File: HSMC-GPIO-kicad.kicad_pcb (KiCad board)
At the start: 2 copper layers, 88.9 x 78.1 mm, 158 parts, among them J1 HSMC, J3 Conn_01x03_Male, J4 I2C, J5 Screw_Terminal_01x04, J6 Conn_02x20_Odd_Even, J7 Conn_02x20_Odd_Even, U2 MC78M05_TO252, U3 TCA9517

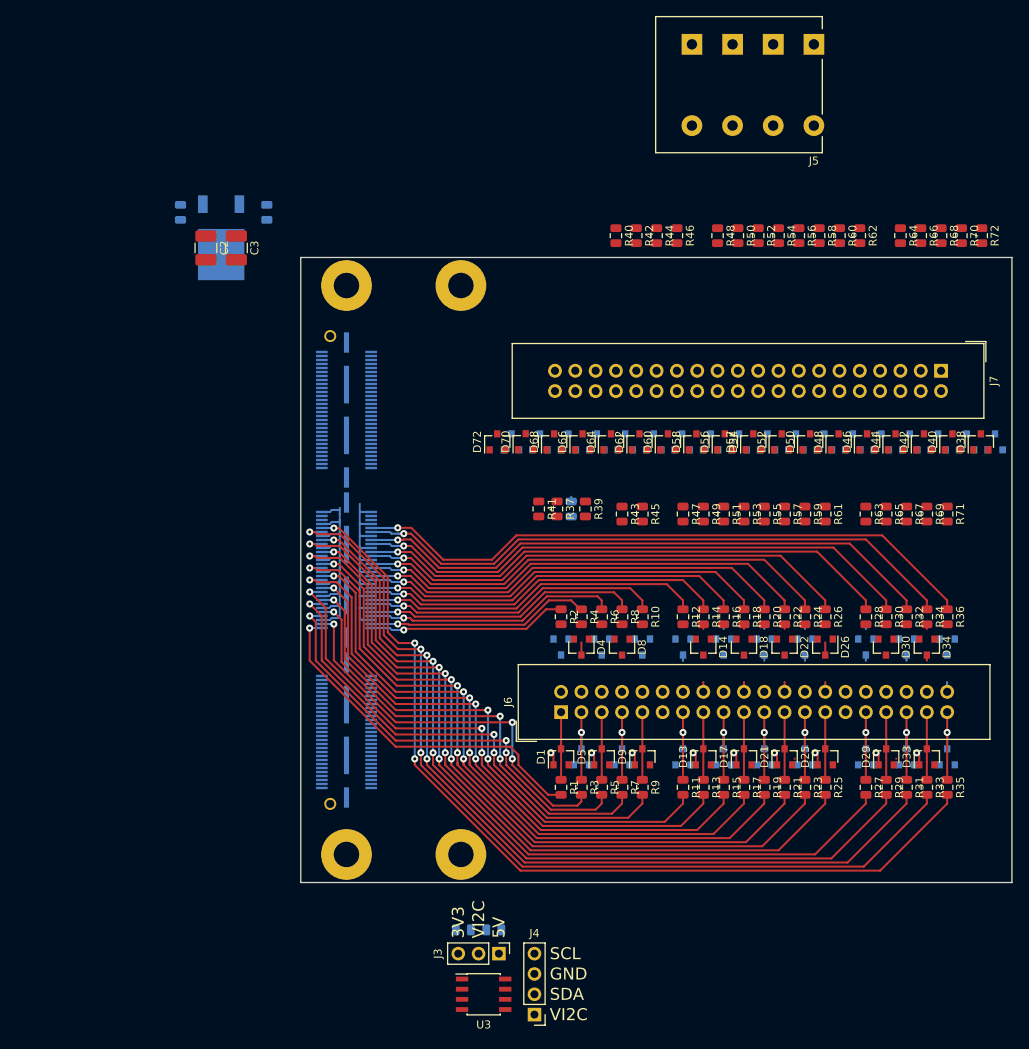
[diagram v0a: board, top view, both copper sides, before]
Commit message: Reroute ribbon connector protection circuitry, switch to single ribbon cable configuration.
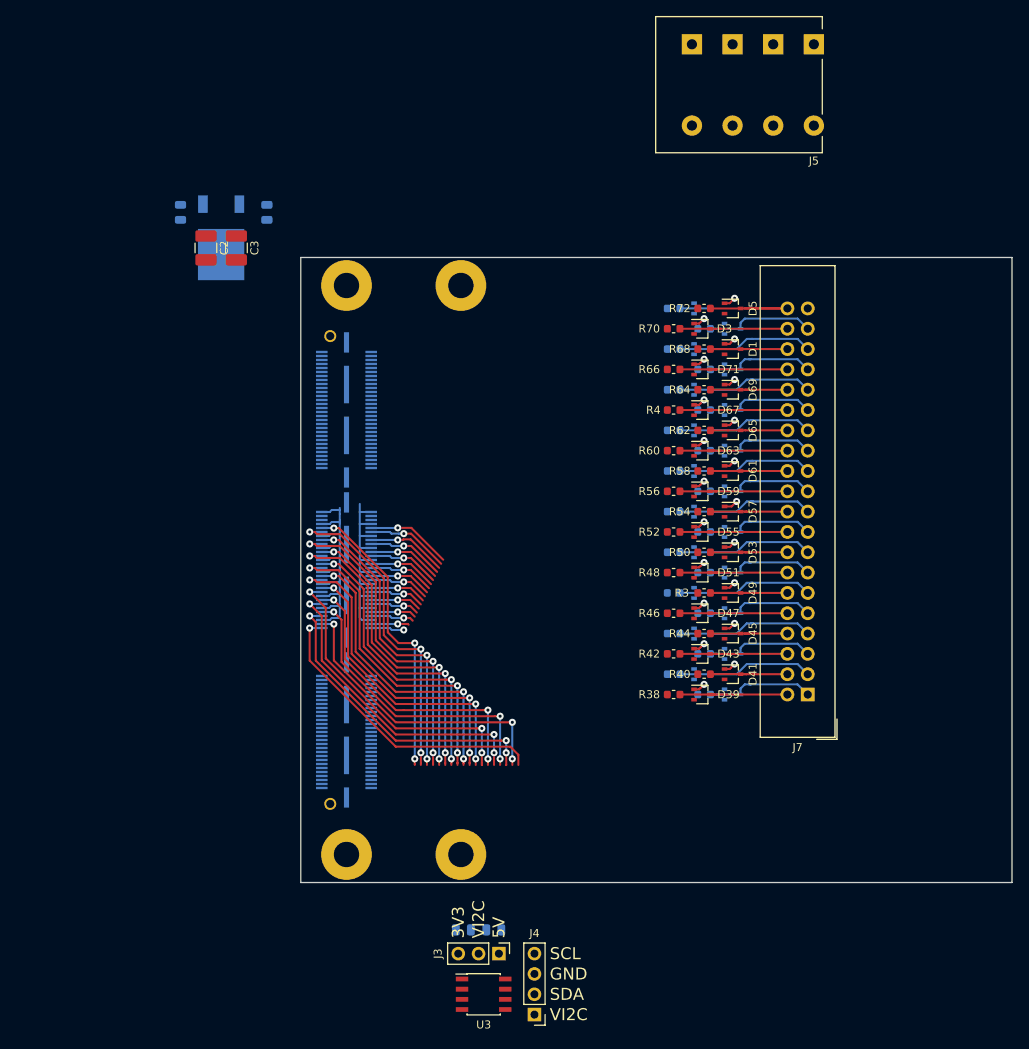
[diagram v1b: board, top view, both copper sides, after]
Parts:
- removed D10, D11, D12, D13, D14, D15, D16, D17, D18, D19, D20, D21, D22, D23, D24, D25, D26, D27, D28, D29, D30, D31, D32, D33, D34, D35, D36, D37, D6, D7, D8, D9: BAT54S, Package_TO_SOT_SMD:SOT-23
- removed J6: Conn_02x20_Odd_Even, Connector_IDC:IDC-Header_2x20_P2.54mm_Vertical
- removed R10, R11, R12, R13, R14, R15, R16, R17, R18, R19, R20, R21, R22, R23, R24, R25, R26, R27, R28, R29, R30, R31, R32, R33, R34, R35, R36, R5, R6, R7, R8, R9: 50, Resistor_SMD:R_0805_2012Metric
- D1, D2, D5: footprint Package_TO_SOT_SMD:SOT-23 -> Package_TO_SOT_SMD:SOT-323_SC-70
- D3, D39, D41, D43, D45, D47, D49, D51, D53, D55, D57, D59, D61, D63, D65, D67, D69, D71: footprint Package_TO_SOT_SMD:SOT-23 -> Package_TO_SOT_SMD:SOT-323_SC-70; moved to F.Cu
- D38, D4, D40, D42, D44, D46, D48, D50, D52, D54, D56, D58, D60, D62, D64, D66, D68, D70, D72: footprint Package_TO_SOT_SMD:SOT-23 -> Package_TO_SOT_SMD:SOT-323_SC-70; moved to B.Cu
- R1, R2, R37, R39, R41, R43, R45, R47, R49, R51, R53, R55, R57, R59, R61, R63, R65, R67, R69, R71: footprint Resistor_SMD:R_0805_2012Metric -> Resistor_SMD:R_0603_1608Metric; moved to B.Cu
- R3, R4, R40, R42, R44, R46, R48, R50, R52, R54, R56, R58, R60, R62, R64, R66, R68, R70, R72: footprint Resistor_SMD:R_0805_2012Metric -> Resistor_SMD:R_0603_1608Metric
- R38: footprint Resistor_SMD:R_0805_2012Metric -> Resistor_SMD:R_0603_1608Metric; moved to F.Cu
- moved D5 58.4 mm to (79.4, 31.8), turned to 0 degrees
- moved R40 55.9 mm to (75.8, 77.5), turned to 0 degrees
- moved D3 55.6 mm to (75.6, 34.3), turned to 0 degrees
- moved D1 55.3 mm to (79.4, 36.9), turned to 0 degrees
- moved R42 52.5 mm to (72.0, 75.0), turned to 0 degrees
- moved R44 50.1 mm to (75.8, 72.4), turned to 0 degrees
- moved R46 47.2 mm to (72.0, 69.9), turned to 0 degrees
- moved D39 45.7 mm to (75.6, 80.0), turned to 0 degrees
- moved D2 45.2 mm to (79.4, 34.3), turned to 0 degrees
- moved D4 44.9 mm to (75.6, 31.8), turned to 0 degrees
- moved D38 44.3 mm to (79.4, 80.0), turned to 0 degrees
- moved J7 43.8 mm to (88.8, 80.0), turned to 180 degrees
- moved R71 42.8 mm to (72.0, 31.8), turned to 180 degrees
- moved D40 42.7 mm to (75.6, 77.5), turned to 0 degrees
- moved R48 42.5 mm to (72.0, 64.8), turned to 0 degrees
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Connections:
- net Net-(J1-Pad155) renamed /GPIO37
- net Net-(J1-Pad156) renamed /GPIO38
- net Net-(J1-Pad157) renamed /GPIO39
- net Net-(J1-Pad158) renamed /GPIO40
- D1 pad 3: /GPIO A/P0 -> /GPIO B/P36
- D2 pad 3: /GPIO A/P1 -> /GPIO B/P37
- D3 pad 3: /GPIO A/P2 -> /GPIO B/P38
- D4 pad 3: /GPIO A/P3 -> /GPIO B/P39
- D5 pad 3: /GPIO A/P4 -> /GPIO B/P40
- J1 pad 101: /GPIO-B0 -> /GPIO1
- J1 pad 102: /GPIO-B1 -> /GPIO2
- J1 pad 103: /GPIO-B2 -> /GPIO3
- J1 pad 104: /GPIO-B3 -> /GPIO4
- J1 pad 107: /GPIO-B4 -> /GPIO5
- J1 pad 108: /GPIO-B5 -> /GPIO6
- J1 pad 109: /GPIO-B6 -> /GPIO7
- J1 pad 110: /GPIO-B7 -> /GPIO8
- J1 pad 113: /GPIO-B8 -> /GPIO9
- J1 pad 114: /GPIO-B9 -> /GPIO10
- J1 pad 115: /GPIO-B10 -> /GPIO11
- J1 pad 116: /GPIO-B11 -> /GPIO12
- J1 pad 119: /GPIO-B12 -> /GPIO13
- J1 pad 120: /GPIO-B13 -> /GPIO14
- J1 pad 121: /GPIO-B14 -> /GPIO15
- J1 pad 122: /GPIO-B15 -> /GPIO16
- J1 pad 125: /GPIO-B16 -> /GPIO17
- J1 pad 126: /GPIO-B17 -> /GPIO18
- J1 pad 127: /GPIO-B18 -> /GPIO19
- J1 pad 128: /GPIO-B19 -> /GPIO20
- J1 pad 131: /GPIO-B20 -> /GPIO21
- J1 pad 132: /GPIO-B21 -> /GPIO22
- J1 pad 133: /GPIO-B22 -> /GPIO23
- J1 pad 134: /GPIO-B23 -> /GPIO24
- J1 pad 137: /GPIO-B24 -> /GPIO25
- J1 pad 138: /GPIO-B25 -> /GPIO26
- J1 pad 139: /GPIO-B26 -> /GPIO27
- J1 pad 140: /GPIO-B27 -> /GPIO28
- J1 pad 143: /GPIO-B28 -> /GPIO29
- J1 pad 144: /GPIO-B29 -> /GPIO30
- J1 pad 145: /GPIO-B30 -> /GPIO31
- J1 pad 146: /GPIO-B31 -> /GPIO32
- J1 pad 149: /GPIO-B32 -> /GPIO33
- J1 pad 150: /GPIO-B33 -> /GPIO34
- J1 pad 151: /GPIO-B34 -> /GPIO35
- J1 pad 152: /GPIO-B35 -> /GPIO36
- J7 pad 1: /GPIO B/P0 -> /GPIO B/P1
- J7 pad 10: /GPIO B/P9 -> /GPIO B/P10
- J7 pad 11: +5V -> /GPIO B/P11
- J7 pad 12: GND -> /GPIO B/P12
- J7 pad 13: /GPIO B/P10 -> /GPIO B/P13
- J7 pad 14: /GPIO B/P11 -> /GPIO B/P14
- J7 pad 15: /GPIO B/P12 -> /GPIO B/P15
- J7 pad 16: /GPIO B/P13 -> /GPIO B/P16
- J7 pad 17: /GPIO B/P14 -> /GPIO B/P17
- J7 pad 18: /GPIO B/P15 -> /GPIO B/P18
- J7 pad 19: /GPIO B/P16 -> /GPIO B/P19
- J7 pad 2: /GPIO B/P1 -> /GPIO B/P2
- J7 pad 20: /GPIO B/P17 -> /GPIO B/P20
- J7 pad 21: /GPIO B/P18 -> /GPIO B/P21
- J7 pad 22: /GPIO B/P19 -> /GPIO B/P22
- J7 pad 23: /GPIO B/P20 -> /GPIO B/P23
- J7 pad 24: /GPIO B/P21 -> /GPIO B/P24
- J7 pad 25: /GPIO B/P22 -> /GPIO B/P25
- J7 pad 26: /GPIO B/P23 -> /GPIO B/P26
- J7 pad 27: /GPIO B/P24 -> /GPIO B/P27
- J7 pad 28: /GPIO B/P25 -> /GPIO B/P28
- J7 pad 29: +3V3 -> /GPIO B/P29
- J7 pad 3: /GPIO B/P2 -> /GPIO B/P3
- J7 pad 30: GND -> /GPIO B/P30
- J7 pad 31: /GPIO B/P26 -> /GPIO B/P31
- J7 pad 32: /GPIO B/P27 -> /GPIO B/P32
- J7 pad 33: /GPIO B/P28 -> /GPIO B/P33
- J7 pad 34: /GPIO B/P29 -> /GPIO B/P34
- J7 pad 35: /GPIO B/P30 -> /GPIO B/P35
- J7 pad 36: /GPIO B/P31 -> /GPIO B/P36
- J7 pad 37: /GPIO B/P32 -> /GPIO B/P37
- J7 pad 38: /GPIO B/P33 -> /GPIO B/P38
- J7 pad 39: /GPIO B/P34 -> /GPIO B/P39
- J7 pad 4: /GPIO B/P3 -> /GPIO B/P4
- J7 pad 40: /GPIO B/P35 -> /GPIO B/P40
- J7 pad 5: /GPIO B/P4 -> /GPIO B/P5
- J7 pad 6: /GPIO B/P5 -> /GPIO B/P6
- J7 pad 7: /GPIO B/P6 -> /GPIO B/P7
- J7 pad 8: /GPIO B/P7 -> /GPIO B/P8
- J7 pad 9: /GPIO B/P8 -> /GPIO B/P9
- R1 pad 1: /GPIO A/P0 -> /GPIO B/P11
- R1 pad 2: /GPIO-A0 -> /GPIO-B11
- R2 pad 1: /GPIO-A1 -> /GPIO B/P29
- R2 pad 2: /GPIO A/P1 -> /GPIO-B29
- R3 pad 1: /GPIO A/P2 -> /GPIO-B12
- R3 pad 2: /GPIO-A2 -> /GPIO B/P12
- R37 pad 1: /GPIO B/P0 -> /GPIO B/P1
- R37 pad 2: /GPIO-B0 -> /GPIO-B1
- R38 pad 1: /GPIO-B1 -> /GPIO-B2
- R38 pad 2: /GPIO B/P1 -> /GPIO B/P2
- R39 pad 1: /GPIO B/P2 -> /GPIO B/P3
- R39 pad 2: /GPIO-B2 -> /GPIO-B3
- R4 pad 1: /GPIO-A3 -> /GPIO-B30
- R4 pad 2: /GPIO A/P3 -> /GPIO B/P30
- R40 pad 1: /GPIO-B3 -> /GPIO-B4
- R40 pad 2: /GPIO B/P3 -> /GPIO B/P4
- R41 pad 1: /GPIO B/P4 -> /GPIO B/P5
- R41 pad 2: /GPIO-B4 -> /GPIO-B5
- R42 pad 1: /GPIO-B5 -> /GPIO-B6
- R42 pad 2: /GPIO B/P5 -> /GPIO B/P6
- R43 pad 1: /GPIO B/P6 -> /GPIO B/P7
- R43 pad 2: /GPIO-B6 -> /GPIO-B7
- R44 pad 1: /GPIO-B7 -> /GPIO-B8
- R44 pad 2: /GPIO B/P7 -> /GPIO B/P8
- R45 pad 1: /GPIO B/P8 -> /GPIO B/P9
- R45 pad 2: /GPIO-B8 -> /GPIO-B9
- R46 pad 1: /GPIO-B9 -> /GPIO-B10
- R46 pad 2: /GPIO B/P9 -> /GPIO B/P10
- R47 pad 1: /GPIO B/P10 -> /GPIO B/P13
- R47 pad 2: /GPIO-B10 -> /GPIO-B13
- R48 pad 1: /GPIO-B11 -> /GPIO-B14
- R48 pad 2: /GPIO B/P11 -> /GPIO B/P14
- R49 pad 1: /GPIO B/P12 -> /GPIO B/P15
- R49 pad 2: /GPIO-B12 -> /GPIO-B15
- R50 pad 1: /GPIO-B13 -> /GPIO-B16
- R50 pad 2: /GPIO B/P13 -> /GPIO B/P16
- R51 pad 1: /GPIO B/P14 -> /GPIO B/P17
- R51 pad 2: /GPIO-B14 -> /GPIO-B17
- R52 pad 1: /GPIO-B15 -> /GPIO-B18
- R52 pad 2: /GPIO B/P15 -> /GPIO B/P18
- R53 pad 1: /GPIO B/P16 -> /GPIO B/P19
- R53 pad 2: /GPIO-B16 -> /GPIO-B19
- R54 pad 1: /GPIO-B17 -> /GPIO-B20
- R54 pad 2: /GPIO B/P17 -> /GPIO B/P20
- R55 pad 1: /GPIO B/P18 -> /GPIO B/P21
- R55 pad 2: /GPIO-B18 -> /GPIO-B21
- R56 pad 1: /GPIO-B19 -> /GPIO-B22
- R56 pad 2: /GPIO B/P19 -> /GPIO B/P22
- R57 pad 1: /GPIO B/P20 -> /GPIO B/P23
- R57 pad 2: /GPIO-B20 -> /GPIO-B23
- R58 pad 1: /GPIO-B21 -> /GPIO-B24
- R58 pad 2: /GPIO B/P21 -> /GPIO B/P24
- R59 pad 1: /GPIO B/P22 -> /GPIO B/P25
- R59 pad 2: /GPIO-B22 -> /GPIO-B25
- R60 pad 1: /GPIO-B23 -> /GPIO-B26
- R60 pad 2: /GPIO B/P23 -> /GPIO B/P26
- R61 pad 1: /GPIO B/P24 -> /GPIO B/P27
- R61 pad 2: /GPIO-B24 -> /GPIO-B27
- R62 pad 1: /GPIO-B25 -> /GPIO-B28
- R62 pad 2: /GPIO B/P25 -> /GPIO B/P28
- R63 pad 1: /GPIO B/P26 -> /GPIO B/P31
- R63 pad 2: /GPIO-B26 -> /GPIO-B31
- R64 pad 1: /GPIO-B27 -> /GPIO-B32
- R64 pad 2: /GPIO B/P27 -> /GPIO B/P32
- R65 pad 1: /GPIO B/P28 -> /GPIO B/P33
- R65 pad 2: /GPIO-B28 -> /GPIO-B33
- R66 pad 1: /GPIO-B29 -> /GPIO-B34
- R66 pad 2: /GPIO B/P29 -> /GPIO B/P34
- R67 pad 1: /GPIO B/P30 -> /GPIO B/P35
- R67 pad 2: /GPIO-B30 -> /GPIO-B35
- R68 pad 1: /GPIO-B31 -> /GPIO-B36
- R68 pad 2: /GPIO B/P31 -> /GPIO B/P36
- R69 pad 1: /GPIO B/P32 -> /GPIO B/P37
- R69 pad 2: /GPIO-B32 -> /GPIO-B37
- R70 pad 1: /GPIO-B33 -> /GPIO-B38
- R70 pad 2: /GPIO B/P33 -> /GPIO B/P38
- R71 pad 1: /GPIO B/P34 -> /GPIO B/P39
- R71 pad 2: /GPIO-B34 -> /GPIO-B39
- R72 pad 1: /GPIO-B35 -> /GPIO-B40
- R72 pad 2: /GPIO B/P35 -> /GPIO B/P40
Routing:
- net /GPIO-A34: track 113.5 -> 36.9 mm
- net /GPIO-A32: track 113.0 -> 40.1 mm
- net /GPIO-A30: track 106.2 -> 37.0 mm
- net /GPIO-A35: track 79.4 -> 10.7 mm
- net /GPIO-A33: track 76.6 -> 10.4 mm
- net /GPIO-A28: track 105.6 -> 40.2 mm
- net /GPIO-A31: track 73.7 -> 10.00 mm
- net /GPIO-A26: track 98.7 -> 37.0 mm
- net /GPIO-A29: track 70.9 -> 9.69 mm
- net /GPIO-A27: track 68.0 -> 9.23 mm
- net /GPIO-A24: track 95.7 -> 40.2 mm
- net /GPIO-A25: track 62.7 -> 8.98 mm
- net /GPIO-A22: track 88.8 -> 37.1 mm
- net /GPIO-A23: track 59.7 -> 8.52 mm
- net /GPIO-A21: track 57.0 -> 8.27 mm
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
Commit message: Change pin/bus labels in schematic
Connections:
- net /GPIO B/P1 renamed /GPIO/P1
- net /GPIO B/P10 renamed /GPIO/P10
- net /GPIO B/P11 renamed /GPIO/P11
- net /GPIO B/P12 renamed /GPIO/P12
- net /GPIO B/P13 renamed /GPIO/P13
- net /GPIO B/P14 renamed /GPIO/P14
- net /GPIO B/P15 renamed /GPIO/P15
- net /GPIO B/P16 renamed /GPIO/P16
- net /GPIO B/P17 renamed /GPIO/P17
- net /GPIO B/P18 renamed /GPIO/P18
- net /GPIO B/P19 renamed /GPIO/P19
- net /GPIO B/P2 renamed /GPIO/P2
- net /GPIO B/P20 renamed /GPIO/P20
- net /GPIO B/P21 renamed /GPIO/P21
- net /GPIO B/P22 renamed /GPIO/P22
- net /GPIO B/P23 renamed /GPIO/P23
- net /GPIO B/P24 renamed /GPIO/P24
- net /GPIO B/P25 renamed /GPIO/P25
- net /GPIO B/P26 renamed /GPIO/P26
- net /GPIO B/P27 renamed /GPIO/P27
- net /GPIO B/P28 renamed /GPIO/P28
- net /GPIO B/P29 renamed /GPIO/P29
- net /GPIO B/P3 renamed /GPIO/P3
- net /GPIO B/P30 renamed /GPIO/P30
- net /GPIO B/P31 renamed /GPIO/P31
- net /GPIO B/P32 renamed /GPIO/P32
- net /GPIO B/P33 renamed /GPIO/P33
- net /GPIO B/P34 renamed /GPIO/P34
- net /GPIO B/P35 renamed /GPIO/P35
- net /GPIO B/P36 renamed /GPIO/P36
- net /GPIO B/P37 renamed /GPIO/P37
- net /GPIO B/P38 renamed /GPIO/P38
- net /GPIO B/P39 renamed /GPIO/P39
- net /GPIO B/P4 renamed /GPIO/P4
- net /GPIO B/P40 renamed /GPIO/P40
- net /GPIO B/P5 renamed /GPIO/P5
- net /GPIO B/P6 renamed /GPIO/P6
- net /GPIO B/P7 renamed /GPIO/P7
- net /GPIO B/P8 renamed /GPIO/P8
- net /GPIO B/P9 renamed /GPIO/P9
- J1 pad 101: /GPIO1 -> /GPIO0
- J1 pad 102: /GPIO2 -> /GPIO1
- J1 pad 103: /GPIO3 -> /GPIO2
- J1 pad 104: /GPIO4 -> /GPIO3
- J1 pad 107: /GPIO5 -> /GPIO4
- J1 pad 108: /GPIO6 -> /GPIO5
- J1 pad 109: /GPIO7 -> /GPIO6
- J1 pad 110: /GPIO8 -> /GPIO7
- J1 pad 113: /GPIO9 -> /GPIO8
- J1 pad 114: /GPIO10 -> /GPIO9
- J1 pad 115: /GPIO11 -> /GPIO10
- J1 pad 116: /GPIO12 -> /GPIO11
- J1 pad 119: /GPIO13 -> /GPIO12
- J1 pad 120: /GPIO14 -> /GPIO13
- J1 pad 121: /GPIO15 -> /GPIO14
- J1 pad 122: /GPIO16 -> /GPIO15
- J1 pad 125: /GPIO17 -> /GPIO16
- J1 pad 126: /GPIO18 -> /GPIO17
- J1 pad 127: /GPIO19 -> /GPIO18
- J1 pad 128: /GPIO20 -> /GPIO19
- J1 pad 131: /GPIO21 -> /GPIO20
- J1 pad 132: /GPIO22 -> /GPIO21
- J1 pad 133: /GPIO23 -> /GPIO22
- J1 pad 134: /GPIO24 -> /GPIO23
- J1 pad 137: /GPIO25 -> /GPIO24
- J1 pad 138: /GPIO26 -> /GPIO25
- J1 pad 139: /GPIO27 -> /GPIO26
- J1 pad 140: /GPIO28 -> /GPIO27
- J1 pad 143: /GPIO29 -> /GPIO28
- J1 pad 144: /GPIO30 -> /GPIO29
- J1 pad 145: /GPIO31 -> /GPIO30
- J1 pad 146: /GPIO32 -> /GPIO31
- J1 pad 149: /GPIO33 -> /GPIO32
- J1 pad 150: /GPIO34 -> /GPIO33
- J1 pad 151: /GPIO35 -> /GPIO34
- J1 pad 152: /GPIO36 -> /GPIO35
- J1 pad 155: /GPIO37 -> /GPIO36
- J1 pad 156: /GPIO38 -> /GPIO37
- J1 pad 157: /GPIO39 -> /GPIO38
- J1 pad 158: /GPIO40 -> /GPIO39
- R1 pad 2: /GPIO-B11 -> /GPIO10
- R2 pad 2: /GPIO-B29 -> /GPIO28
- R3 pad 1: /GPIO-B12 -> /GPIO11
- R37 pad 2: /GPIO-B1 -> /GPIO0
- R38 pad 1: /GPIO-B2 -> /GPIO1
- R39 pad 2: /GPIO-B3 -> /GPIO2
- R4 pad 1: /GPIO-B30 -> /GPIO29
- R40 pad 1: /GPIO-B4 -> /GPIO3
- R41 pad 2: /GPIO-B5 -> /GPIO4
- R42 pad 1: /GPIO-B6 -> /GPIO5
- R43 pad 2: /GPIO-B7 -> /GPIO6
- R44 pad 1: /GPIO-B8 -> /GPIO7
- R45 pad 2: /GPIO-B9 -> /GPIO8
- R46 pad 1: /GPIO-B10 -> /GPIO9
- R47 pad 2: /GPIO-B13 -> /GPIO12
- R48 pad 1: /GPIO-B14 -> /GPIO13
- R49 pad 2: /GPIO-B15 -> /GPIO14
- R50 pad 1: /GPIO-B16 -> /GPIO15
- R51 pad 2: /GPIO-B17 -> /GPIO16
- R52 pad 1: /GPIO-B18 -> /GPIO17
- R53 pad 2: /GPIO-B19 -> /GPIO18
- R54 pad 1: /GPIO-B20 -> /GPIO19
- R55 pad 2: /GPIO-B21 -> /GPIO20
- R56 pad 1: /GPIO-B22 -> /GPIO21
- R57 pad 2: /GPIO-B23 -> /GPIO22
- R58 pad 1: /GPIO-B24 -> /GPIO23
- R59 pad 2: /GPIO-B25 -> /GPIO24
- R60 pad 1: /GPIO-B26 -> /GPIO25
- R61 pad 2: /GPIO-B27 -> /GPIO26
- R62 pad 1: /GPIO-B28 -> /GPIO27
- R63 pad 2: /GPIO-B31 -> /GPIO30
- R64 pad 1: /GPIO-B32 -> /GPIO31
- R65 pad 2: /GPIO-B33 -> /GPIO32
- R66 pad 1: /GPIO-B34 -> /GPIO33
- R67 pad 2: /GPIO-B35 -> /GPIO34
- R68 pad 1: /GPIO-B36 -> /GPIO35
- R69 pad 2: /GPIO-B37 -> /GPIO36
- R70 pad 1: /GPIO-B38 -> /GPIO37
- R71 pad 2: /GPIO-B39 -> /GPIO38
- R72 pad 1: /GPIO-B40 -> /GPIO39

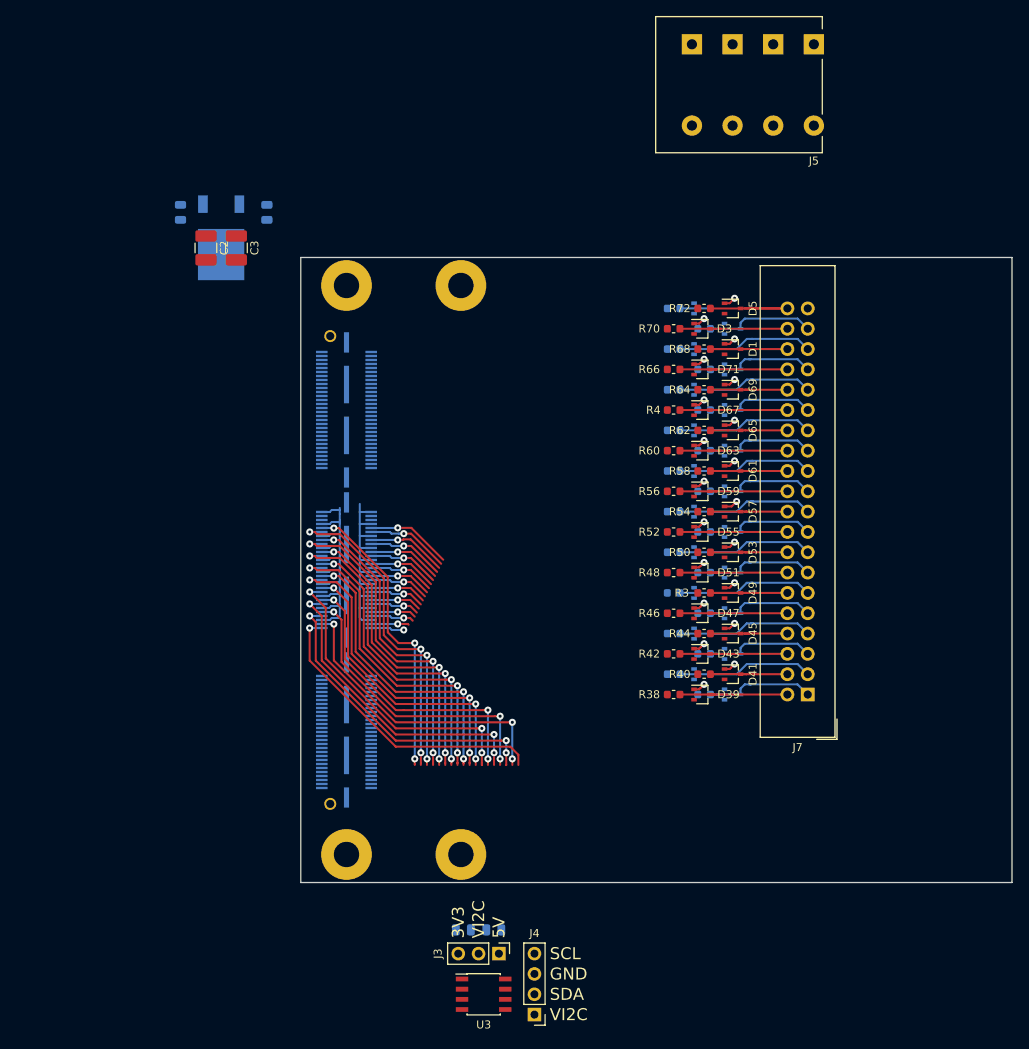
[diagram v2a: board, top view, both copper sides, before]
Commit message: Begin routing ribbon cable connector
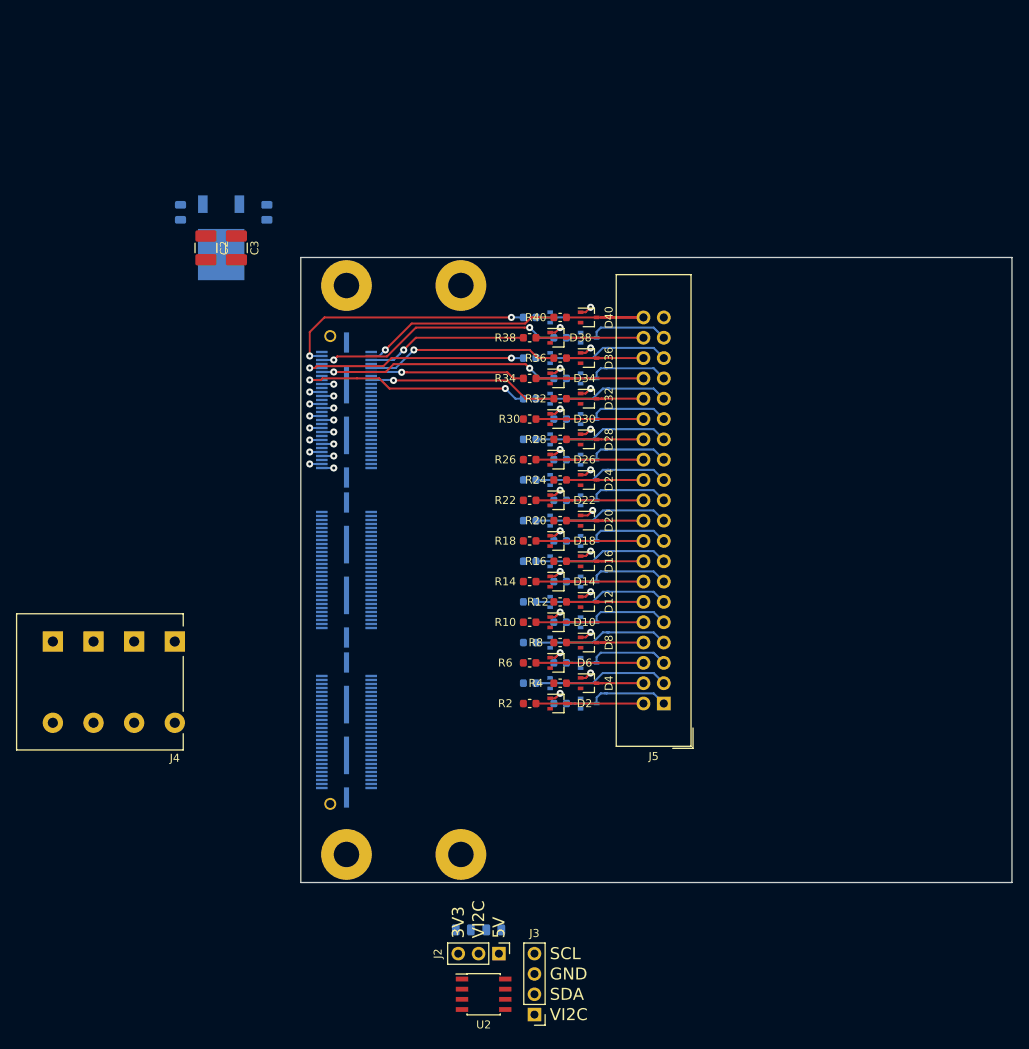
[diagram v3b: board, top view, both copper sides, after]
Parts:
- moved J4 109.3 mm to (9.65, 83.6)
- moved D10 18.0 mm to (57.6, 71.0)
- moved D11 18.0 mm to (57.6, 68.5)
- moved D14 18.0 mm to (57.6, 65.9)
- moved D15 18.0 mm to (57.6, 63.4)
- moved D18 18.0 mm to (57.6, 60.8)
- moved D19 18.0 mm to (57.6, 58.3)
- moved D2 18.0 mm to (57.6, 81.2)
- moved D22 18.0 mm to (57.6, 55.8)
- moved D23 18.0 mm to (57.6, 53.2)
- moved D26 18.0 mm to (57.6, 50.7)
- moved D27 18.0 mm to (57.6, 48.1)
- moved D3 18.0 mm to (57.6, 78.6)
- moved D30 18.0 mm to (57.6, 45.6)
- moved D31 18.0 mm to (57.6, 43.1)
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- renumbered D38 to D1, D47 to D10, D48 to D11, D49 to D12, D50 to D13, D51 to D14, D52 to D15, D53 to D16, D54 to D17, D55 to D18, D56 to D19, D39 to D2, D57 to D20, D58 to D21, D59 to D22, D60 to D23, D61 to D24, D62 to D25, D63 to D26, D64 to D27, D65 to D28, D66 to D29, D40 to D3, D67 to D30, D68 to D31, D69 to D32, D70 to D33, D71 to D34, D72 to D35, D1 to D36, D2 to D37, D3 to D38, D4 to D39, D41 to D4, D5 to D40, D42 to D5, D43 to D6, D44 to D7, D45 to D8, D46 to D9, J3 to J2, J4 to J3, J5 to J4, J7 to J5, R37 to R1, R46 to R10, R1 to R11, R3 to R12, R47 to R13, R48 to R14, R49 to R15, R50 to R16, R51 to R17, R52 to R18, R53 to R19, R38 to R2, R54 to R20, R55 to R21, R56 to R22, R57 to R23, R58 to R24, R59 to R25, R60 to R26, R61 to R27, R62 to R28, R2 to R29, R39 to R3, R4 to R30, R63 to R31, R64 to R32, R65 to R33, R66 to R34, R67 to R35, R68 to R36, R69 to R37, R70 to R38, R71 to R39, R40 to R4, R72 to R40, R41 to R5, R42 to R6, R43 to R7, R44 to R8, R45 to R9, U2 to U1, U3 to U2
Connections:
- net /GPIO-A0 renamed Net-(J1-Pad41)
- net /GPIO-A1 renamed Net-(J1-Pad42)
- net /GPIO-A10 renamed Net-(J1-Pad55)
- net /GPIO-A11 renamed Net-(J1-Pad56)
- net /GPIO-A12 renamed Net-(J1-Pad59)
- net /GPIO-A13 renamed Net-(J1-Pad60)
- net /GPIO-A14 renamed Net-(J1-Pad61)
- net /GPIO-A15 renamed Net-(J1-Pad62)
- net /GPIO-A16 renamed Net-(J1-Pad65)
- net /GPIO-A17 renamed Net-(J1-Pad66)
- net /GPIO-A18 renamed Net-(J1-Pad67)
- net /GPIO-A19 renamed Net-(J1-Pad68)
- net /GPIO-A2 renamed Net-(J1-Pad43)
- net /GPIO-A20 renamed Net-(J1-Pad71)
- net /GPIO-A21 renamed Net-(J1-Pad72)
- net /GPIO-A22 renamed Net-(J1-Pad73)
- net /GPIO-A23 renamed Net-(J1-Pad74)
- net /GPIO-A24 renamed Net-(J1-Pad77)
- net /GPIO-A25 renamed Net-(J1-Pad78)
- net /GPIO-A26 renamed Net-(J1-Pad79)
- net /GPIO-A27 renamed Net-(J1-Pad80)
- net /GPIO-A28 renamed Net-(J1-Pad83)
- net /GPIO-A29 renamed Net-(J1-Pad84)
- net /GPIO-A3 renamed Net-(J1-Pad44)
- net /GPIO-A30 renamed Net-(J1-Pad85)
- net /GPIO-A31 renamed Net-(J1-Pad86)
- net /GPIO-A32 renamed Net-(J1-Pad89)
- net /GPIO-A33 renamed Net-(J1-Pad90)
- net /GPIO-A34 renamed Net-(J1-Pad91)
- net /GPIO-A35 renamed Net-(J1-Pad92)
- net /GPIO-A4 renamed Net-(J1-Pad47)
- net /GPIO-A5 renamed Net-(J1-Pad48)
- net /GPIO-A6 renamed Net-(J1-Pad49)
- net /GPIO-A7 renamed Net-(J1-Pad50)
- net /GPIO-A8 renamed Net-(J1-Pad53)
- net /GPIO-A9 renamed Net-(J1-Pad54)
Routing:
- net Net-(J1-Pad77): track 40.2 -> 0.00 mm, vias 3 -> 0
- net Net-(J1-Pad83): track 40.2 -> 0.00 mm, vias 3 -> 0
- net Net-(J1-Pad71): track 40.2 -> 0.00 mm, vias 3 -> 0
- net Net-(J1-Pad89): track 40.1 -> 0.00 mm, vias 3 -> 0
- net Net-(J1-Pad65): track 40.1 -> 0.00 mm, vias 3 -> 0
- net +3V3: track 38.4 -> 0.00 mm
- net Net-(J1-Pad47): track 38.4 -> 0.00 mm, vias 3 -> 0
- net Net-(J1-Pad53): track 38.4 -> 0.00 mm, vias 3 -> 0
- net Net-(J1-Pad59): track 38.3 -> 0.00 mm, vias 3 -> 0
- net Net-(J1-Pad41): track 37.8 -> 0.00 mm, vias 1 -> 0
- net Net-(J1-Pad67): track 37.2 -> 0.00 mm, vias 3 -> 0
- net Net-(J1-Pad73): track 37.1 -> 0.00 mm, vias 3 -> 0
- net Net-(J1-Pad79): track 37.0 -> 0.00 mm, vias 3 -> 0
- net Net-(J1-Pad85): track 37.0 -> 0.00 mm, vias 3 -> 0
- net Net-(J1-Pad43): track 36.9 -> 0.00 mm, vias 3 -> 0
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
